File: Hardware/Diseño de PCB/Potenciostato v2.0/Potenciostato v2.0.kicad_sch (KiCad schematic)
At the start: 31 parts, among them J1 Conn_Coaxial, J2 Conn_02x15_Odd_Even, J3 Conn_Coaxial, J5 Conn_Coaxial, J7 USB_B_Micro, U6 AMS1117-3.3, U7 AMS1117-5.0

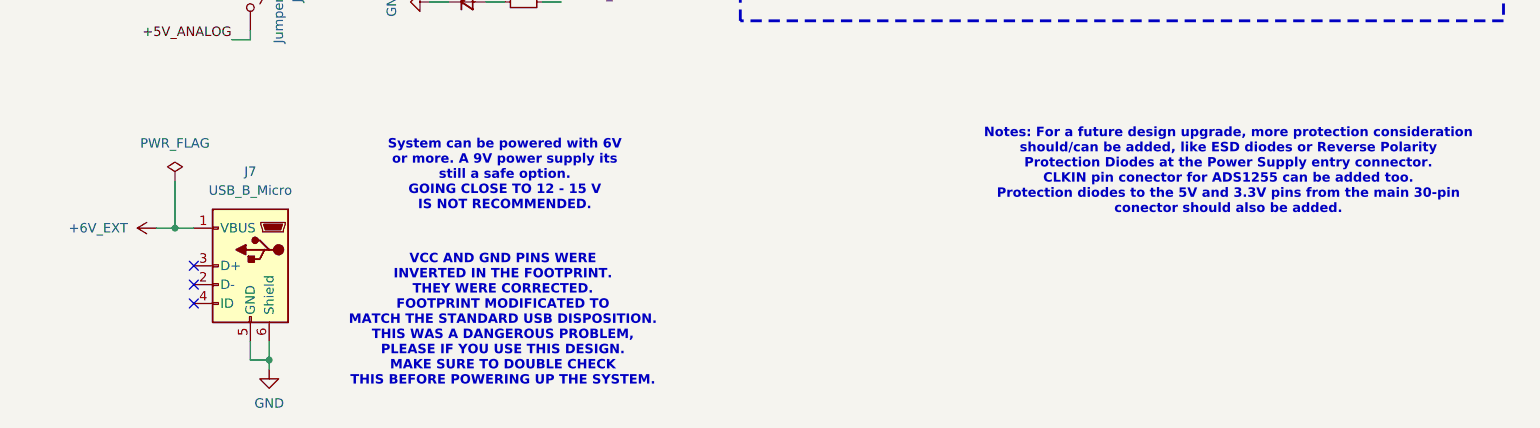
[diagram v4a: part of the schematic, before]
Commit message: Hardware: Hardware Corrections in Potentiostat, small but important ones (WE electrode, Normal Open connection for electric disconnection in schematic and PCB. DAC I2C pull up resistors connected to 5V PCB layout corrected.). New project for ESP32 board: board design to hold ESP32 and LevelShifter for I2C3.3V to 5V. No more. No big changes in firmware and software, nothing to note, really small corrections in that were in the way.
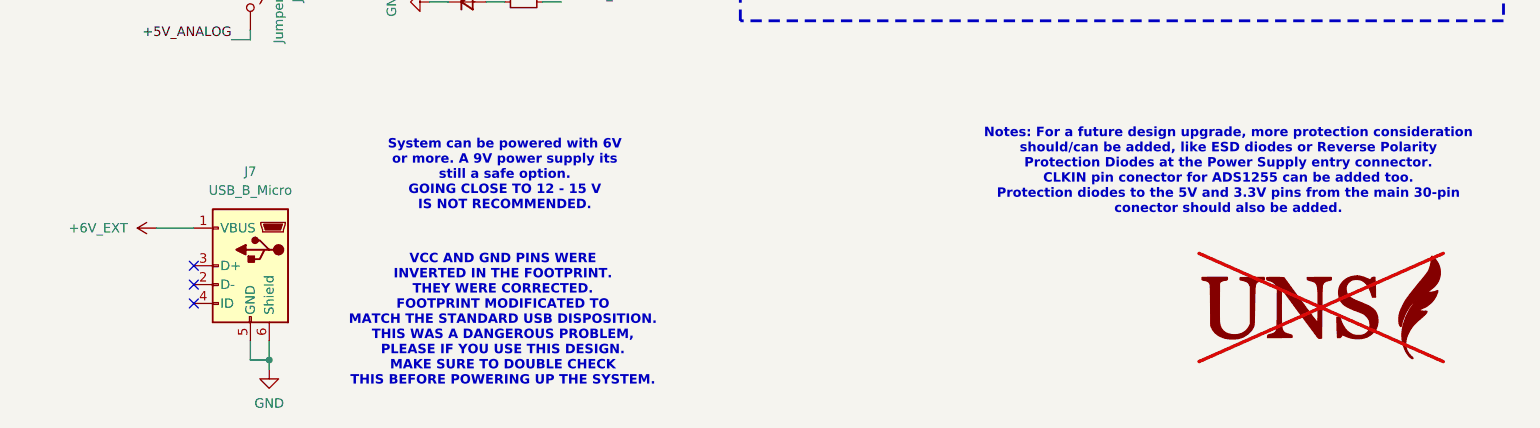
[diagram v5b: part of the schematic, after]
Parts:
- added U8: ~, symbol Graphics_images:UNS_logo
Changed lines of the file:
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@@
 	)
 	(junction
-		(at 102.87 162.56)
-		(diameter 0)
-		(color 0 0 0 0)
-	)
-	(junction
 		(at 247.65 59.69)
 		(diameter 0)
@@
 	(wire
 		(pts
-			(xy 100.33 162.56) (xy 102.87 162.56)
+			(xy 100.33 162.56) (xy 105.41 162.56)
 		)
 		(stroke
@@
 	(wire
 		(pts
-			(xy 102.87 162.56) (xy 105.41 162.56)
-		)
-		(stroke
-			(width 0)
-			(type default)
-		)
-	)
-	(wire
-		(pts
 			(xy 101.6 110.49) (xy 105.41 110.49)
 		)
@@
 	(wire
 		(pts
-			(xy 102.87 156.21) (xy 102.87 162.56)
-		)
-		(stroke
-			(width 0)
-			(type default)
-		)
-	)
-	(wire
-		(pts
 			(xy 110.49 123.19) (xy 113.03 123.19)
 		)
@@
 	)
 	(symbol
-		(lib_id "power:PWR_FLAG")
-		(at 102.87 156.21 0)
-		(unit 1)
-		(exclude_from_sim no)
-		(in_bom yes)
-		(on_board yes)
-		(dnp no)
-		(fields_autoplaced yes)
-		(property "Reference" "#FLG01"
-			(at 102.87 154.305 0)
-			(effects
-				(font
-					(size 1.27 1.27)
-				)
-				(hide yes)
-			)
-		)
-		(property "Value" "PWR_FLAG"
-			(at 102.87 151.13 0)
-			(effects
-				(font
-					(size 1.27 1.27)
-				)
-			)
-		)
-		(property "Footprint" ""
-			(at 102.87 156.21 0)
-			(effects
-				(font
-					(size 1.27 1.27)
-				)
-				(hide yes)
-			)
-		)
-		(property "Datasheet" "~"
-			(at 102.87 156.21 0)
-			(effects
-				(font
-					(size 1.27 1.27)
-				)
-				(hide yes)
-			)
-		)
-		(property "Description" "Special symbol for telling ERC where power comes from"
-			(at 102.87 156.21 0)
-			(effects
-				(font
-					(size 1.27 1.27)
-				)
-				(hide yes)
-			)
-		)
-		(pin "1"
-		)
-		(instances
-			(project "Potenciostato v2.0"
-				(path "/3273751a-bb69-4014-b380-866ff743e010"
-					(reference "#FLG01")
-					(unit 1)
-				)
-			)
-		)
-	)
-	(symbol
 		(lib_id "Connector:Conn_Coaxial")
 		(at 133.35 110.49 0)
@@
 					(unit 1)
 				)
+			)
+		)
+	)
+	(symbol
+		(lib_id "Graphics_images:UNS_logo")
+		(at 241.3 166.37 0)
+		(unit 1)
+		(exclude_from_sim no)
+		(in_bom no)
+		(on_board no)
+		(dnp yes)
+		(fields_autoplaced yes)
+		(property "Reference" "U8"
+			(at 240.538 161.798 0)
+			(effects
+				(font
+					(size 1.27 1.27)
+				)
+				(justify left)
+				(hide yes)
+			)
+		)
+		(property "Value" "~"
+			(at 220.98 157.48 0)
+			(effects
+				(font
+					(size 1.27 1.27)
+				)
+				(justify left)
+			)
+		)
+		(property "Footprint" ""
+			(at 232.41 162.56 0)
+			(effects
+				(font
+					(size 1.27 1.27)
+				)
+				(hide yes)
+			)
+		)
+		(property "Datasheet" ""
+			(at 232.41 162.56 0)
+			(effects
+				(font
+					(size 1.27 1.27)
+				)
+				(hide yes)
+			)
+		)
+		(property "Description" ""
+			(at 232.41 162.56 0)
+			(effects
+				(font
+					(size 1.27 1.27)
+				)
+				(hide yes)
+			)
+		)
+		(property "JLCLIB" ""
+			(at 241.3 166.37 0)
+			(effects
+				(font
+					(size 1.27 1.27)
+				)
+				(hide yes)
+			)
+		)
+		(instances
+			(project "Potenciostato v2.0"
+				(path "/3273751a-bb69-4014-b380-866ff743e010"
+					(reference "U8")
+					(unit 1)
+				)
